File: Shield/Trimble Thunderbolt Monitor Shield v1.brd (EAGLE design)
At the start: 160 x 100 mm, 31 parts, among them Q1 2N2222, U2 MAX232PTH

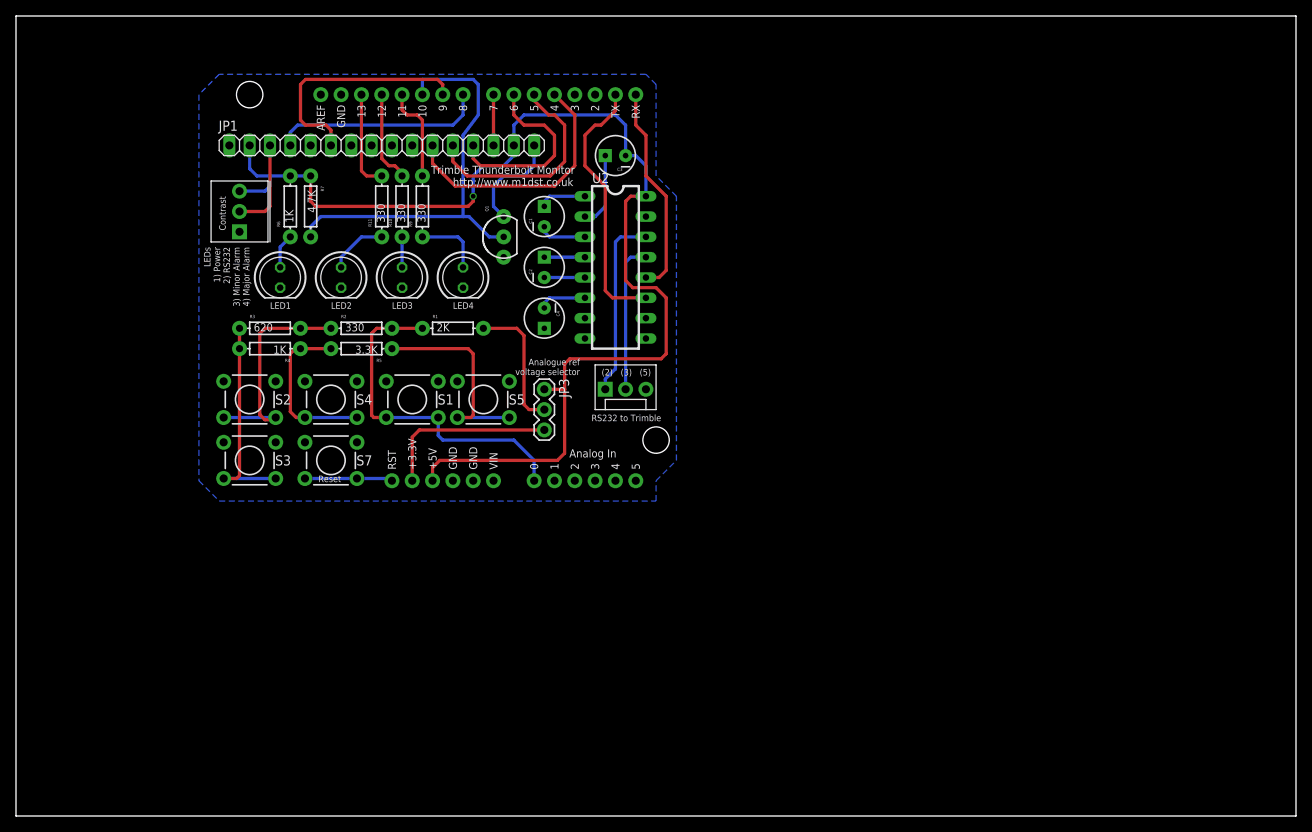
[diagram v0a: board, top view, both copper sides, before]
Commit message: Updated some more silkscreen items, a few traces and added gerber files.
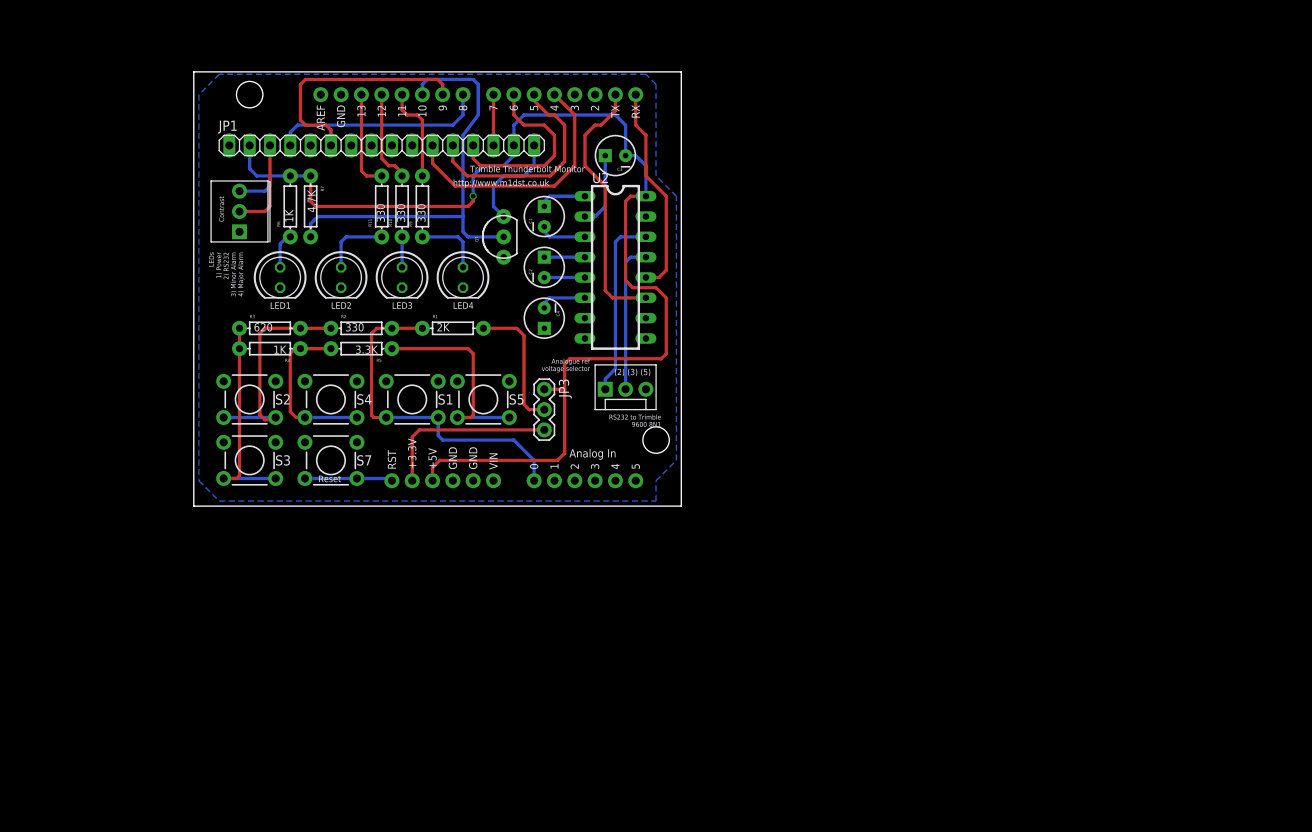
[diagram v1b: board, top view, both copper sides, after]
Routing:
- net LEDRS232: track 7.40 -> 8.52 mm
- net D10: track 53.3 -> 54.2 mm
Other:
- board size 160 x 100 mm -> 60.9 x 54.3 mm
- board text added: "RS232 to Trimble 9600 8N1"
- board text removed: "RS232 to Trimble"
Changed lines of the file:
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@@
 <board>
 <plain>
-<wire x1="0" y1="0" x2="160" y2="0" width="0" layer="20"/>
-<wire x1="160" y1="0" x2="160" y2="100" width="0" layer="20"/>
-<wire x1="160" y1="100" x2="0" y2="100" width="0" layer="20"/>
-<wire x1="0" y1="100" x2="0" y2="0" width="0" layer="20"/>
-<text x="69.85" y="81.28" size="1.016" layer="21" rot="R180">Trimble Thunderbolt Monitor</text>
-<text x="54.61" y="78.74" size="1.016" layer="21">http://www.m1dst.co.uk</text>
-<text x="57.785" y="74.295" size="1.778" layer="22" rot="MR0">http://www.m1dst.co.uk</text>
-<text x="70.485" y="57.15" size="0.8128" layer="21" rot="R180">Analogue ref
+<wire x1="22.225" y1="38.735" x2="83.165" y2="38.735" width="0" layer="20"/>
+<wire x1="83.165" y1="38.735" x2="83.165" y2="93.015" width="0" layer="20"/>
+<wire x1="83.165" y1="93.015" x2="22.225" y2="93.015" width="0" layer="20"/>
+<wire x1="22.225" y1="93.015" x2="22.225" y2="38.735" width="0" layer="20"/>
+<text x="71.12" y="81.28" size="0.8128" layer="21" font="vector" rot="R180">Trimble Thunderbolt Monitor</text>
+<text x="54.61" y="78.74" size="0.8128" layer="21" font="vector">http://www.m1dst.co.uk</text>
+<text x="58.42" y="74.295" size="1.6764" layer="22" font="vector" rot="MR0">http://www.m1dst.co.uk</text>
+<text x="71.755" y="57.15" size="0.6096" layer="21" font="vector" rot="R180">Analogue ref
 voltage selector</text>
-<text x="80.645" y="50.165" size="0.8128" layer="21" rot="R180">RS232 to Trimble</text>
+<text x="80.645" y="50.165" size="0.6096" layer="21" font="vector" rot="R180">RS232 to Trimble
+9600 8N1</text>
 <text x="40.64" y="42.545" size="0.8128" layer="21" rot="R180">Reset</text>
-<text x="25.4" y="77.47" size="0.8128" layer="21" rot="R270">Contrast</text>
-<text x="23.495" y="71.12" size="0.8128" layer="21" rot="R270">LEDs
+<text x="25.4" y="77.47" size="0.6096" layer="21" font="vector" rot="R270">Contrast</text>
+<text x="24.13" y="70.485" size="0.6096" layer="21" font="vector" rot="R270">LEDs
 1) Power
 2) RS232
 3) Minor Alarm
 4) Major Alarm</text>
-<text x="79.375" y="55.88" size="0.8128" layer="21" rot="R180">(2)   (3)   (5)</text>
+<text x="79.375" y="55.88" size="0.762" layer="21" font="vector" rot="R180">(2) (3) (5)</text>
 </plain>
 <attributes>
@@
 <element name="TRIMLCD" library="SparkFun" package="3362U" value="10K" x="30.48" y="73.025" rot="R90"/>
 <element name="R7" library="SparkFun" package="AXIAL-0.3" value="4.7K" x="36.83" y="76.2" rot="R270"/>
-<element name="Q1" library="SparkFun" package="TO-92-AMMO" value="2N2222" x="60.96" y="72.39" rot="R90"/>
+<element name="Q1" library="SparkFun" package="TO-92-AMMO" value="2N2222" x="60.96" y="72.39" smashed="yes" rot="R90">
+<attribute name="NAME" x="57.785" y="71.755" size="0.4064" layer="25" ratio="10" rot="R90"/>
+<attribute name="VALUE" x="59.69" y="71.755" size="0.4064" layer="27" ratio="10" rot="R90"/>
+</element>
 <element name="JP2" library="SparkFun" package="MOLEX-1X3" value="RS232 (TRIMBLE)" x="73.66" y="53.34" smashed="yes"/>
 <element name="C1" library="SparkFun" package="CPOL-RADIAL-10UF-25V" value="1uF" x="66.04" y="74.93" rot="R90"/>
@@
 <contactref element="LED1" pad="A"/>
 <contactref element="R6" pad="P$1"/>
-<wire x1="33.02" y1="68.58" x2="33.02" y2="71.12" width="0.4064" layer="16"/>
-<wire x1="33.02" y1="71.12" x2="34.29" y2="72.39" width="0.4064" layer="16"/>
+<wire x1="34.29" y1="72.39" x2="33.918025" y2="72.39" width="0.4064" layer="16"/>
+<wire x1="33.918025" y1="72.39" x2="33.02" y2="71.491975" width="0.4064" layer="16"/>
+<wire x1="33.02" y1="71.491975" x2="33.02" y2="68.58" width="0.4064" layer="16"/>
 </signal>
 <signal name="+5V">
@@
 <contactref element="R7" pad="P$2"/>
 <contactref element="Q1" pad="2"/>
-<wire x1="36.83" y1="72.39" x2="36.83" y2="73.66" width="0.4064" layer="16"/>
-<wire x1="36.83" y1="73.66" x2="38.1" y2="74.93" width="0.4064" layer="16"/>
-<wire x1="38.1" y1="74.93" x2="55.88" y2="74.93" width="0.4064" layer="16"/>
-<wire x1="55.88" y1="74.93" x2="56.62395" y2="74.93" width="0.4064" layer="16"/>
-<wire x1="56.62395" y1="74.93" x2="59.16395" y2="72.39" width="0.4064" layer="16"/>
-<wire x1="59.16395" y1="72.39" x2="60.96" y2="72.39" width="0.4064" layer="16"/>
-<wire x1="50.8" y1="90.17" x2="50.8" y2="92.075" width="0.4064" layer="16"/>
-<wire x1="50.8" y1="92.075" x2="57.15" y2="92.075" width="0.4064" layer="16"/>
+<wire x1="36.83" y1="72.39" x2="36.83" y2="74.031975" width="0.4064" layer="16"/>
+<wire x1="36.83" y1="74.031975" x2="37.728025" y2="74.93" width="0.4064" layer="16"/>
+<wire x1="37.728025" y1="74.93" x2="55.88" y2="74.93" width="0.4064" layer="16"/>
+<wire x1="50.8" y1="90.17" x2="50.8" y2="91.44" width="0.4064" layer="16"/>
+<wire x1="50.8" y1="91.44" x2="51.435" y2="92.075" width="0.4064" layer="16"/>
+<wire x1="51.435" y1="92.075" x2="57.15" y2="92.075" width="0.4064" layer="16"/>
 <wire x1="57.15" y1="92.075" x2="57.785" y2="91.44" width="0.4064" layer="16"/>
 <wire x1="57.785" y1="91.44" x2="57.785" y2="87.63" width="0.4064" layer="16"/>
 <wire x1="57.785" y1="87.63" x2="55.88" y2="85.09" width="0.4064" layer="16"/>
 <wire x1="55.88" y1="85.09" x2="55.88" y2="74.93" width="0.4064" layer="16"/>
+<wire x1="60.96" y1="72.39" x2="56.515" y2="72.39" width="0.4064" layer="16"/>
+<wire x1="56.515" y1="72.39" x2="55.88" y2="73.025" width="0.4064" layer="16"/>
+<wire x1="55.88" y1="73.025" x2="55.88" y2="74.93" width="0.4064" layer="16"/>
 </signal>
 <signal name="D11">
@@
 <contactref element="LED2" pad="A"/>
 <contactref element="R11" pad="P$1"/>
-<wire x1="45.72" y1="72.39" x2="43.18" y2="72.39" width="0.4064" layer="16"/>
-<wire x1="43.18" y1="72.39" x2="40.64" y2="69.85" width="0.4064" layer="16"/>
-<wire x1="40.64" y1="69.85" x2="40.64" y2="68.58" width="0.4064" layer="16"/>
+<wire x1="45.72" y1="72.39" x2="41.275" y2="72.39" width="0.4064" layer="16"/>
+<wire x1="41.275" y1="72.39" x2="40.64" y2="71.755" width="0.4064" layer="16"/>
+<wire x1="40.64" y1="71.755" x2="40.64" y2="68.58" width="0.4064" layer="16"/>
 </signal>
 <signal name="D12">
